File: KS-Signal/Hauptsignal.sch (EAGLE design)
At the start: 10 parts

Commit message: ZwischenS1
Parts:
- added IC1: ATTINY44SSU, Attiny:ATTINY44SSU
- added R1, R2, R3, R4, R5, R6, R7, R8, R9: (no value), rcl:R-EU_R0603
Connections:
- net N$1 renamed GN
- new net GE: LED9.A
- new net N$1: LED9.C, R9.1
- new net N$2: LED6.C, R6.1
- new net N$3: LED8.C, R5.1
- new net N$4: LED5.C, R4.1
- new net N$5: LED10.C, R3.1
- new net N$6: LED7.C, R2.1
- new net N$7: LED1.C, R1.1
- new net N$8: LED3.C, LED4.C, R7.1
- new net N$9: LED2.C, R8.1
- new net RT: LED2.A
- new net SH1: LED7.A
- new net SH1ZS1: LED1.A
- new net ZL: LED6.A
- new net ZS7: LED10.A, LED5.A, LED8.A
- net GND: now also R1.2, R2.2, R3.2, R4.2, R5.2, R6.2, R7.2, R8.2, R9.2; no longer LED1.C, LED10.C, LED2.C, LED3.C, LED4.C, LED5.C, LED6.C, LED7.C, LED8.C, LED9.C
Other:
- moved on the sheet: LED1, LED10, LED2, LED3, LED4, LED5, LED6, LED7, LED8, LED9

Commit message: Rückseite fertig
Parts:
- added Q1: IRLML5203, transistor-power:IRLML5203
- added R10: (no value), rcl:R-EU_R0603
- added X1: SSW-106-02-S-S-RA, con-samtec:SSW-106-02-S-S-RA
- added X2: TSW-106-02-S-S-RA, con-samtec:TSW-106-02-S-S-RA
- LED1, LED10, LED5, LED6, LED7, LED8: value LED_SMD3MM -> LED_SMD3MM_SMD/DIP; device LEDFLATTOP:LED_SMD3MM -> LEDFLATTOP:LED_SMD3MM_SMD/DIP
- LED2, LED3, LED4, LED9: value LED_SMD5MM -> LED_SMD5MM_SMD; device LEDFLATTOP:LED_SMD5MM -> LEDFLATTOP:LED_SMD5MM_SMD
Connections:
- new net MISO: IC1G$1.(MISO)PA5, X1-2.1, X2-2.1
- new net N$10: LED10.A, LED5.A, LED8.A, Q1.D
- new net N$11: Q1.G, R10.2
- new net RESET: IC1G$1.PB3(RESET), X1-5.1, X2-5.1
- new net SCL/SCK: IC1G$1.(SCL/SCK)PA4, X1-3.1, X2-3.1
- new net SDA/MOSI: IC1G$1.(SDA/MOSI)PA6, X1-6.1, X2-6.1
- new net VCC: Q1.S, X1-4.1, X2-4.1
- net GE: now also IC1G$1.PA1
- net GN: now also IC1G$1.PA2
- net GND: now also X1-1.1, X2-1.1
- net N$1: now also LED4.C
- net N$8: no longer LED4.C
- net RT: now also IC1G$1.PA3
- net SH1: now also IC1G$1.PB2
- net SH1ZS1: now also IC1G$1.PB1(XTAL2)
- net ZL: now also IC1G$1.PA7
- net ZS7: now also IC1G$1.PB0(XTAL1), R10.1; no longer LED10.A, LED5.A, LED8.A
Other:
- moved on the sheet: IC1G$1, R7

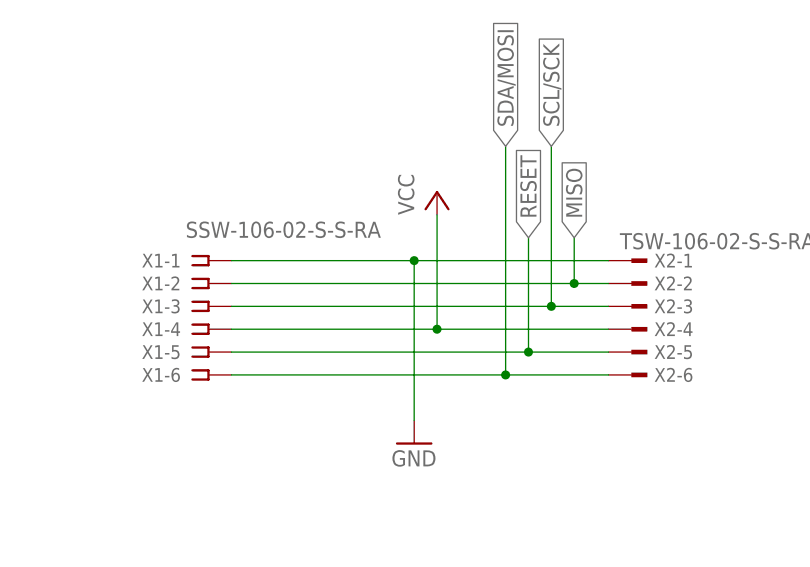
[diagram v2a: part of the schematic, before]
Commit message: Optimierung der Zusatzanzeiger & Hauptsignalplatine
- Symmetrischere Auslegung
- Entfernen von MISO/MISO connection zwischen Zusatzanzeiger und Hauptsignalschirm!
-> Zusatzanzeiger-MISO auf Signalschirmplatine nicht mehr connected (NC)
->mögliches Auslesen des DCC-Signals über den MISO-Anschluss (MOSI und SCK für I2C)
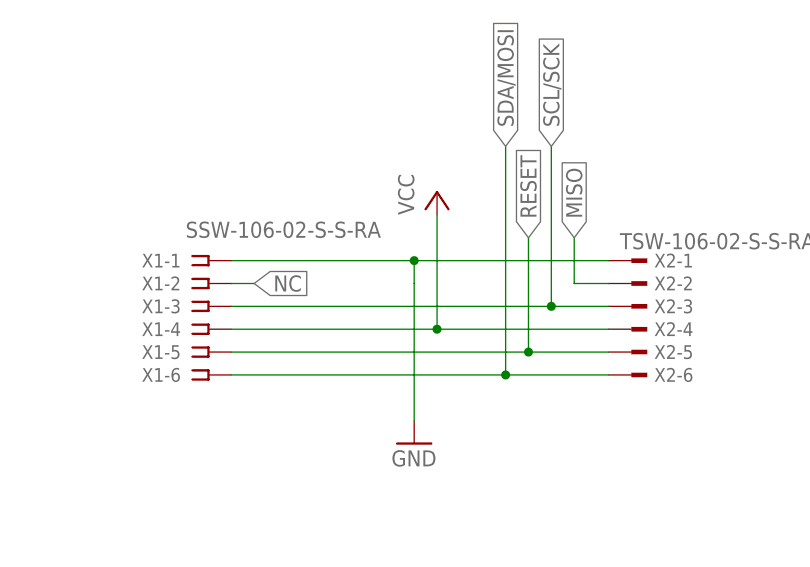
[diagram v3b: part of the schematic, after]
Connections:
- new net NC: X1-2.1
- net MISO: no longer X1-2.1
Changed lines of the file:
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@@
 <?xml version="1.0" encoding="utf-8"?>
 <!DOCTYPE eagle SYSTEM "eagle.dtd">
-<eagle version="8.3.2">
+<eagle version="8.2.2">
 <drawing>
 <settings>
 <setting alwaysvectorfont="no"/>
-<setting keepoldvectorfont="yes"/>
 <setting verticaltext="up"/>
 </settings>
@@
 <net name="MISO" class="0">
 <segment>
-<pinref part="X1" gate="-2" pin="1"/>
 <pinref part="X2" gate="-2" pin="1"/>
-<wire x1="223.52" y1="55.88" x2="261.62" y2="55.88" width="0.1524" layer="91"/>
 <wire x1="261.62" y1="55.88" x2="265.43" y2="55.88" width="0.1524" layer="91"/>
 <wire x1="261.62" y1="55.88" x2="261.62" y2="60.96" width="0.1524" layer="91"/>
-<junction x="261.62" y="55.88"/>
 <label x="261.62" y="60.96" size="1.778" layer="95" rot="R90" xref="yes"/>
 </segment>
@@
 </segment>
 </net>
+<net name="NC" class="0">
+<segment>
+<pinref part="X1" gate="-2" pin="1"/>
+<wire x1="223.52" y1="55.88" x2="226.06" y2="55.88" width="0.1524" layer="91"/>
+<label x="226.06" y="55.88" size="1.778" layer="95" xref="yes"/>
+</segment>
+</net>
